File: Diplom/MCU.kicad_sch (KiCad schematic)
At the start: 50 parts, among them IC1 E22-900T22D, J2 Conn_01x04_Pin, SW1 SW_Push, SW2 SW_Push, U2 BME280, U3 W25Q32JVSS, U6 STM32F411CEUx, Y3 ABM3-25.000MHz-D2Y-T, Y4 KX-327NHT, Y5 Crystal

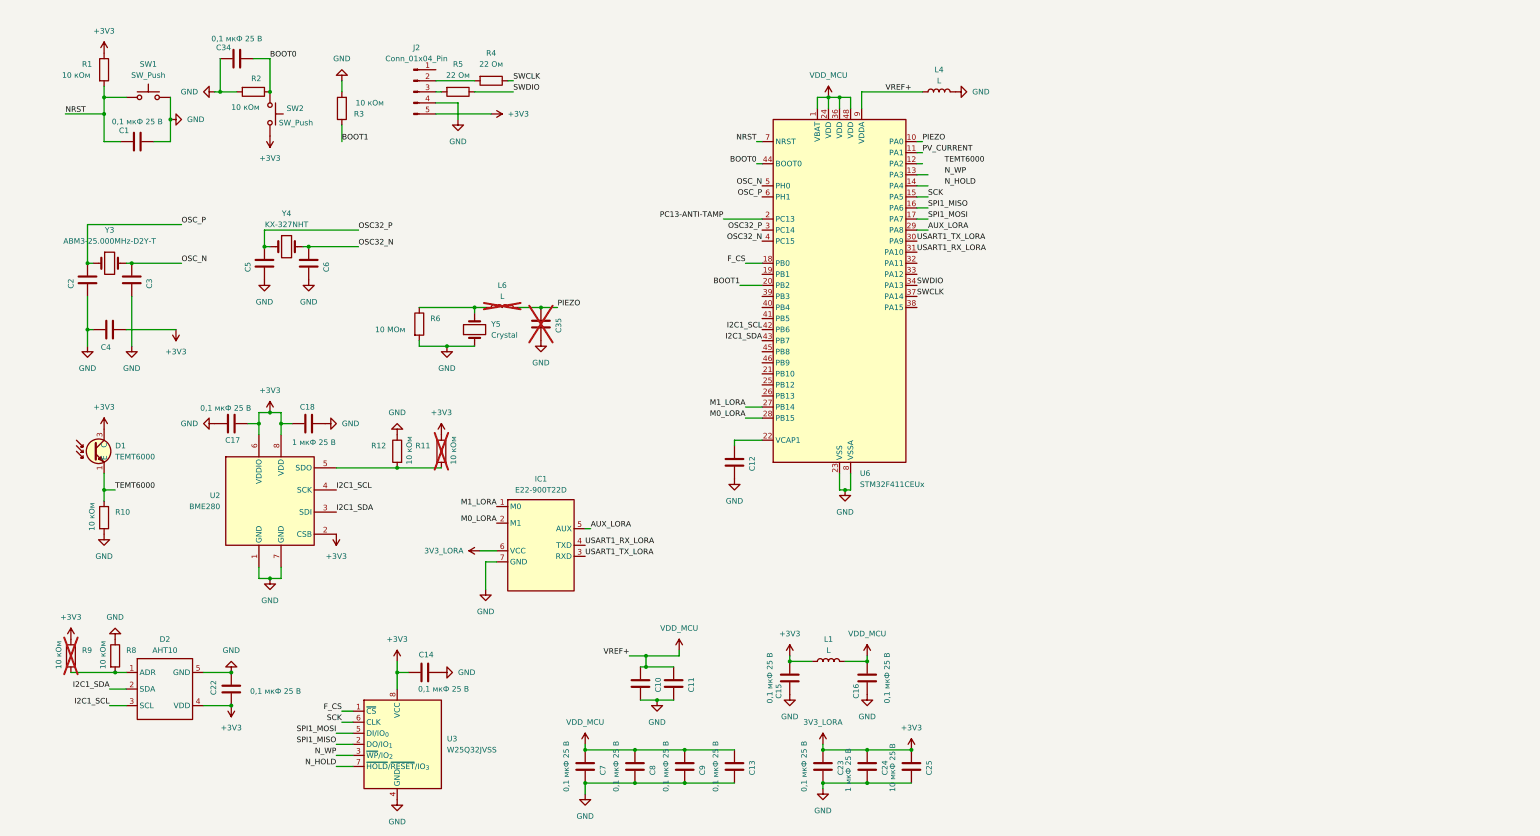
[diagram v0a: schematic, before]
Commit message: version 2.0 fix buttons, roots, tighten dimension
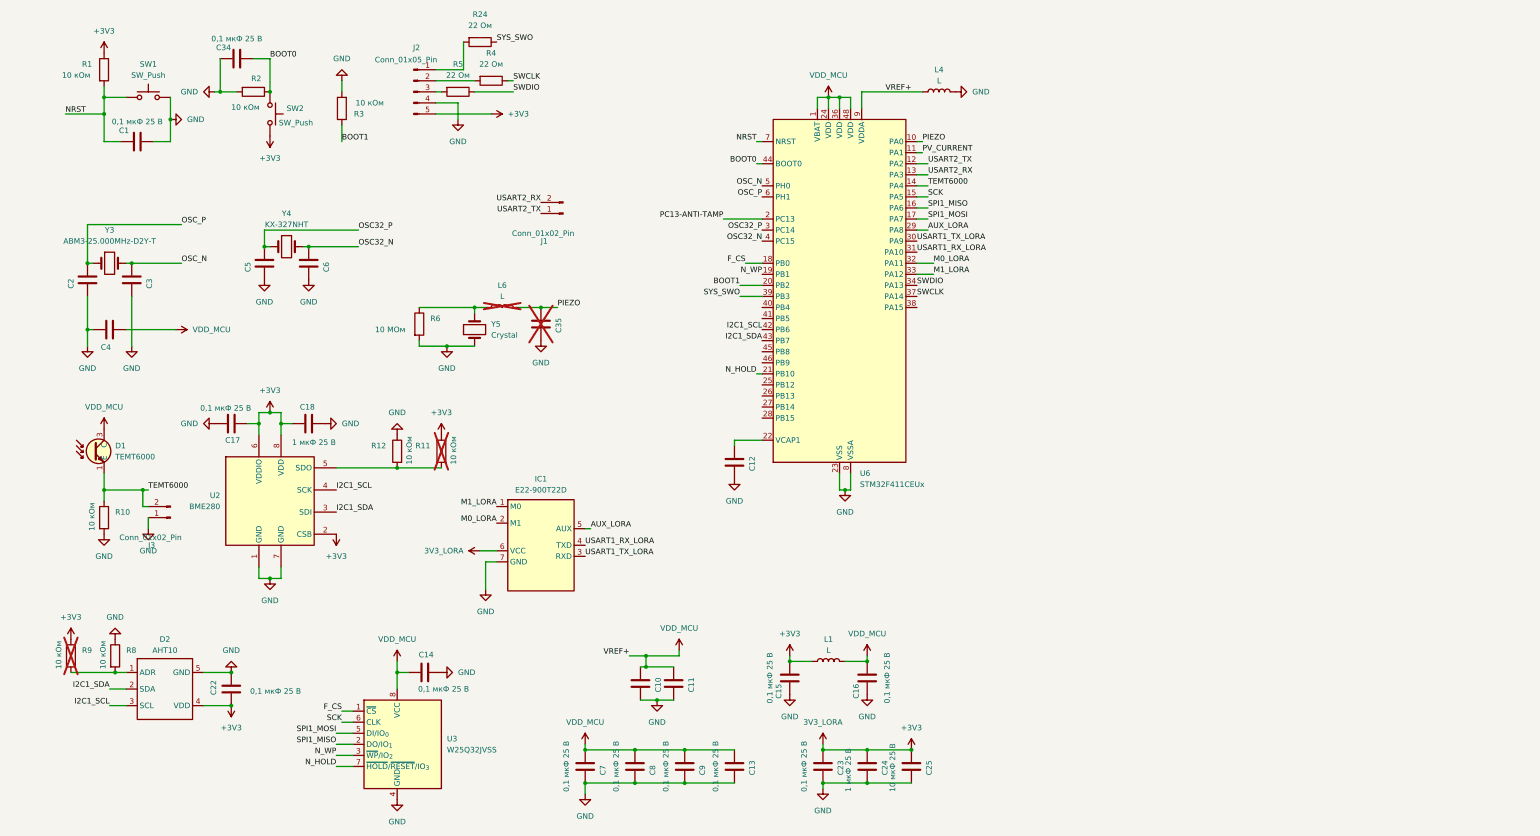
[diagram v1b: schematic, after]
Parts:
- added J1, J3: Conn_01x02_Pin, Connector_PinHeader_2.54mm:PinHeader_1x02_P2.54mm_Vertical, symbol Connector:Conn_01x02_Pin
- added R24: 22 Ом, Resistor_SMD:R_0603_1608Metric_Pad0.98x0.95mm_HandSolder, symbol Device:R
- J2: value Conn_01x04_Pin -> Conn_01x05_Pin; footprint Connector_PinHeader_2.54mm:PinHeader_1x04_P2.54mm_Vertical -> Connector_PinHeader_2.54mm:PinHeader_1x05_P2.54mm_Vertical
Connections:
- net +3V3: no longer C14.1, C4.1, D1.3 (C), U3.8 (VCC)
- net GND: now also J3.1 (Pin_1)
- net M0_LORA: now also U6.32 (PA11); no longer U6.28 (PB15)
- net M1_LORA: now also U6.33 (PA12); no longer U6.27 (PB14)
- net N_HOLD: now also U6.21 (PB10)
- net N_WP: now also U6.19 (PB1)
- net TEMT6000: now also U6.14 (PA4), J3.2 (Pin_2)
- net VDD_MCU: now also C14.1, C4.1, D1.3 (C), U3.8 (VCC)
- net USART2_TX: now reaches U6.12 (PA2)
- net USART2_TX: now also J1.1 (Pin_1)
- net USART2_RX: now reaches U6.13 (PA3)
- net USART2_RX: now also J1.2 (Pin_2)
- net SYS_SWO: now reaches U6.39 (PB3)
- net SYS_SWO: now also R24.1
- net at J2.1 (Pin_1): now also R24.2

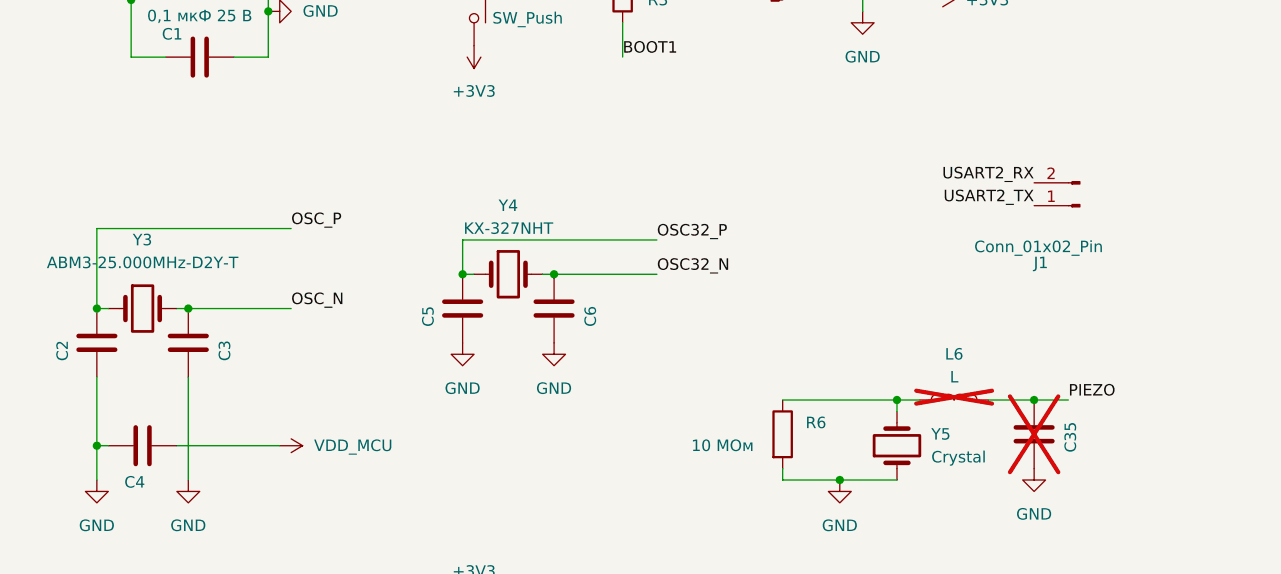
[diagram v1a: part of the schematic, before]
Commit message: Add gitmodule, corrections
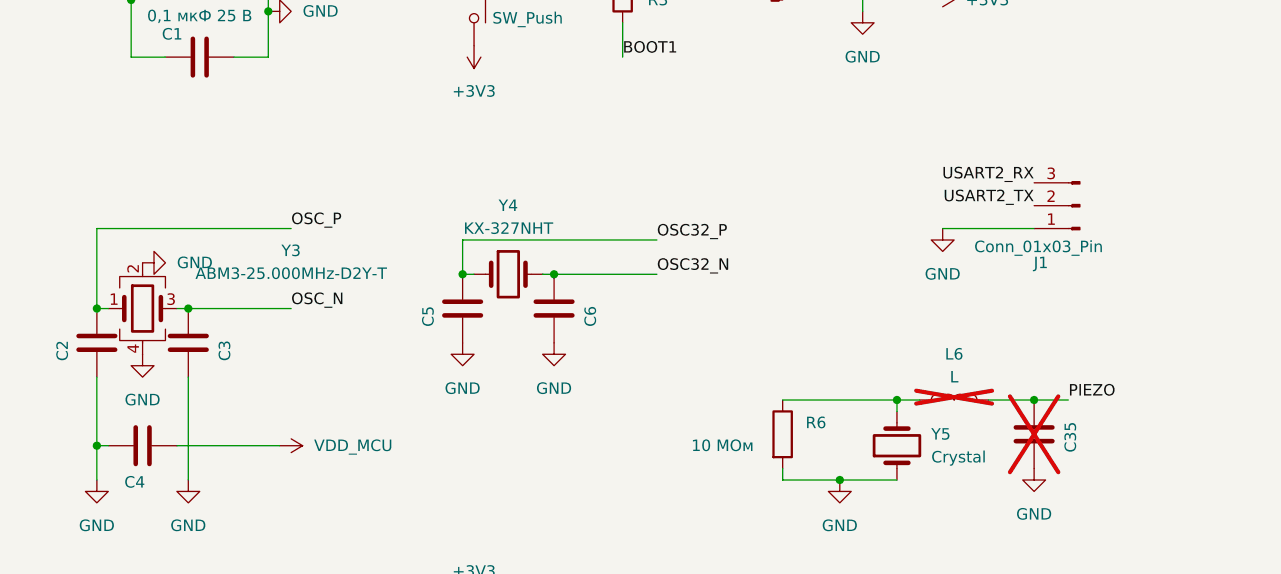
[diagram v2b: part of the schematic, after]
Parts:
- J1: value Conn_01x02_Pin -> Conn_01x03_Pin; footprint Connector_PinHeader_2.54mm:PinHeader_1x02_P2.54mm_Vertical -> Connector_PinHeader_2.54mm:PinHeader_1x03_P2.54mm_Vertical; symbol Connector:Conn_01x02_Pin -> Connector:Conn_01x03_Pin
- SW1, SW2: footprint Button_Switch_THT:SW_PUSH_6mm_H7.3mm -> Diplom:FSM8JSMATR
- Y3: footprint Crystal:Crystal_SMD_3225-4Pin_3.2x2.5mm_HandSoldering -> Crystal:Crystal_SMD_3225-4Pin_3.2x2.5mm; symbol Device:Crystal -> Device:Crystal_GND24
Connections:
- net GND: now also J1.1 (Pin_1), Y3.2, Y3.4
- net OSC_N: now also Y3.3; no longer Y3.2
- net USART2_RX: now also J1.3 (Pin_3); no longer J1.2 (Pin_2)
- net USART2_TX: now also J1.2 (Pin_2); no longer J1.1 (Pin_1)
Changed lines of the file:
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@@
 	(wire
 		(pts
+			(xy 121.92 67.31) (xy 132.08 67.31)
+		)
+		(stroke
+			(width 0)
+			(type default)
+		)
+	)
+	(wire
+		(pts
 			(xy 158.75 176.53) (xy 162.56 176.53)
 		)
@@
 			)
 		)
-		(property "Footprint" "Button_Switch_THT:SW_PUSH_6mm_H7.3mm"
+		(property "Footprint" "Diplom:FSM8JSMATR"
 			(at 74.93 41.91 0)
 			(effects
@@
 			)
 		)
-		(property "Footprint" "Button_Switch_THT:SW_PUSH_6mm_H7.3mm"
+		(property "Footprint" "Diplom:FSM8JSMATR"
 			(at 41.91 33.02 0)
 			(effects
@@
 	)
 	(symbol
+		(lib_id "power:GND")
+		(at 33.02 81.28 0)
+		(unit 1)
+		(exclude_from_sim no)
+		(in_bom yes)
+		(on_board yes)
+		(dnp no)
+		(fields_autoplaced yes)
+		(property "Reference" "#PWR061"
+			(at 33.02 87.63 0)
+			(effects
+				(font
+					(size 1.27 1.27)
+				)
+				(hide yes)
+			)
+		)
+		(property "Value" "GND"
+			(at 33.02 86.36 0)
+			(effects
+				(font
+					(size 1.27 1.27)
+				)
+			)
+		)
+		(property "Footprint" ""
+			(at 33.02 81.28 0)
+			(effects
+				(font
+					(size 1.27 1.27)
+				)
+				(hide yes)
+			)
+		)
+		(property "Datasheet" ""
+			(at 33.02 81.28 0)
+			(effects
+				(font
+					(size 1.27 1.27)
+				)
+				(hide yes)
+			)
+		)
+		(property "Description" "Power symbol creates a global label with name \"GND\" , ground"
+			(at 33.02 81.28 0)
+			(effects
+				(font
+					(size 1.27 1.27)
+				)
+				(hide yes)
+			)
+		)
+		(pin "1"
+		)
+		(instances
+			(project "Diplom"
+				(path "/c3b9ff52-a8d6-450c-a11b-f6a6738b7917/f19e7439-0709-4f6f-9ba2-8e4e7d5c3f4b"
+					(reference "#PWR061")
+					(unit 1)
+				)
+			)
+		)
+	)
+	(symbol
 		(lib_id "Device:R")
 		(at 109.22 119.38 0)
@@
 	)
 	(symbol
-		(lib_id "Device:Crystal")
+		(lib_id "Device:Crystal_GND24")
 		(at 33.02 76.2 0)
 		(unit 1)
@@
 		(fields_autoplaced yes)
 		(property "Reference" "Y3"
-			(at 33.02 68.58 0)
+			(at 49.53 69.7798 0)
 			(effects
 				(font
@@
 		)
 		(property "Value" "ABM3-25.000MHz-D2Y-T"
-			(at 33.02 71.12 0)
+			(at 49.53 72.3198 0)
 			(effects
 				(font
@@
 			)
 		)
-		(property "Footprint" "Crystal:Crystal_SMD_3225-4Pin_3.2x2.5mm_HandSoldering"
+		(property "Footprint" "Crystal:Crystal_SMD_3225-4Pin_3.2x2.5mm"
 			(at 33.02 76.2 0)
 			(effects
@@
 			)
 		)
-		(property "Description" "Two pin crystal 8 MHz"
+		(property "Description" "Four pin crystal, GND on pins 2 and 4"
 			(at 33.02 76.2 0)
 			(effects
@@
 		(pin "1"
 		)
+		(pin "4"
+		)
+		(pin "3"
+		)
 		(instances
 			(project "Diplom"
@@
 	(symbol
 		(lib_id "power:GND")
+		(at 33.02 71.12 90)
+		(unit 1)
+		(exclude_from_sim no)
+		(in_bom yes)
+		(on_board yes)
+		(dnp no)
+		(fields_autoplaced yes)
+		(property "Reference" "#PWR062"
+			(at 39.37 71.12 0)
+			(effects
+				(font
+					(size 1.27 1.27)
+				)
+				(hide yes)
+			)
+		)
+		(property "Value" "GND"
+			(at 36.83 71.1199 90)
+			(effects
+				(font
+					(size 1.27 1.27)
+				)
+				(justify right)
+			)
+		)
+		(property "Footprint" ""
+			(at 33.02 71.12 0)
+			(effects
+				(font
+					(size 1.27 1.27)
+				)
+				(hide yes)
+			)
+		)
+		(property "Datasheet" ""
+			(at 33.02 71.12 0)
+			(effects
+				(font
+					(size 1.27 1.27)
+				)
+				(hide yes)
+			)
+		)
+		(property "Description" "Power symbol creates a global label with name \"GND\" , ground"
+			(at 33.02 71.12 0)
+			(effects
+				(font
+					(size 1.27 1.27)
+				)
+				(hide yes)
+			)
+		)
+		(pin "1"
+		)
+		(instances
+			(project "Diplom"
+				(path "/c3b9ff52-a8d6-450c-a11b-f6a6738b7917/f19e7439-0709-4f6f-9ba2-8e4e7d5c3f4b"
+					(reference "#PWR062")
+					(unit 1)
+				)
+			)
+		)
+	)
+	(symbol
+		(lib_id "power:GND")
 		(at 69.85 148.59 0)
 		(unit 1)
@@
 	)
 	(symbol
+		(lib_id "power:GND")
+		(at 121.92 67.31 0)
+		(unit 1)
+		(exclude_from_sim no)
+		(in_bom yes)
+		(on_board yes)
+		(dnp no)
+		(fields_autoplaced yes)
+		(property "Reference" "#PWR063"
+			(at 121.92 73.66 0)
+			(effects
+				(font
+					(size 1.27 1.27)
+				)
+				(hide yes)
+			)
+		)
+		(property "Value" "GND"
+			(at 121.92 72.39 0)
+			(effects
+				(font
+					(size 1.27 1.27)
+				)
+			)
+		)
+		(property "Footprint" ""
+			(at 121.92 67.31 0)
+			(effects
+				(font
+					(size 1.27 1.27)
+				)
+				(hide yes)
+			)
+		)
+		(property "Datasheet" ""
+			(at 121.92 67.31 0)
+			(effects
+				(font
+					(size 1.27 1.27)
+				)
+				(hide yes)
+			)
+		)
+		(property "Description" "Power symbol creates a global label with name \"GND\" , ground"
+			(at 121.92 67.31 0)
+			(effects
+				(font
+					(size 1.27 1.27)
+				)
+				(hide yes)
+			)
+		)
+		(pin "1"
+		)
+		(instances
+			(project "Diplom"
+				(path "/c3b9ff52-a8d6-450c-a11b-f6a6738b7917/f19e7439-0709-4f6f-9ba2-8e4e7d5c3f4b"
+					(reference "#PWR063")
+					(unit 1)
+				)
+			)
+		)
+	)
+	(symbol
 		(lib_id "Device:L")
 		(at 223.52 36.83 90)
@@
 	)
 	(symbol
-		(lib_id "Connector:Conn_01x02_Pin")
+		(lib_id "Connector:Conn_01x03_Pin")
 		(at 137.16 64.77 180)
 		(unit 1)
@@
 			)
 		)
-		(property "Value" "Conn_01x02_Pin"
+		(property "Value" "Conn_01x03_Pin"
 			(at 132.588 69.342 0)
 			(effects
@@
 			)
 		)
-		(property "Footprint" "Connector_PinHeader_2.54mm:PinHeader_1x02_P2.54mm_Vertical"
+		(property "Footprint" "Connector_PinHeader_2.54mm:PinHeader_1x03_P2.54mm_Vertical"
 			(at 137.16 64.77 0)
 			(effects
@@
 			)
 		)
-		(property "Description" "Generic connector, single row, 01x02, script generated"
+		(property "Description" "Generic connector, single row, 01x03, script generated"
 			(at 137.16 64.77 0)
 			(effects
@@
 		(pin "2"
 		)
+		(pin "3"
+		)
 		(instances

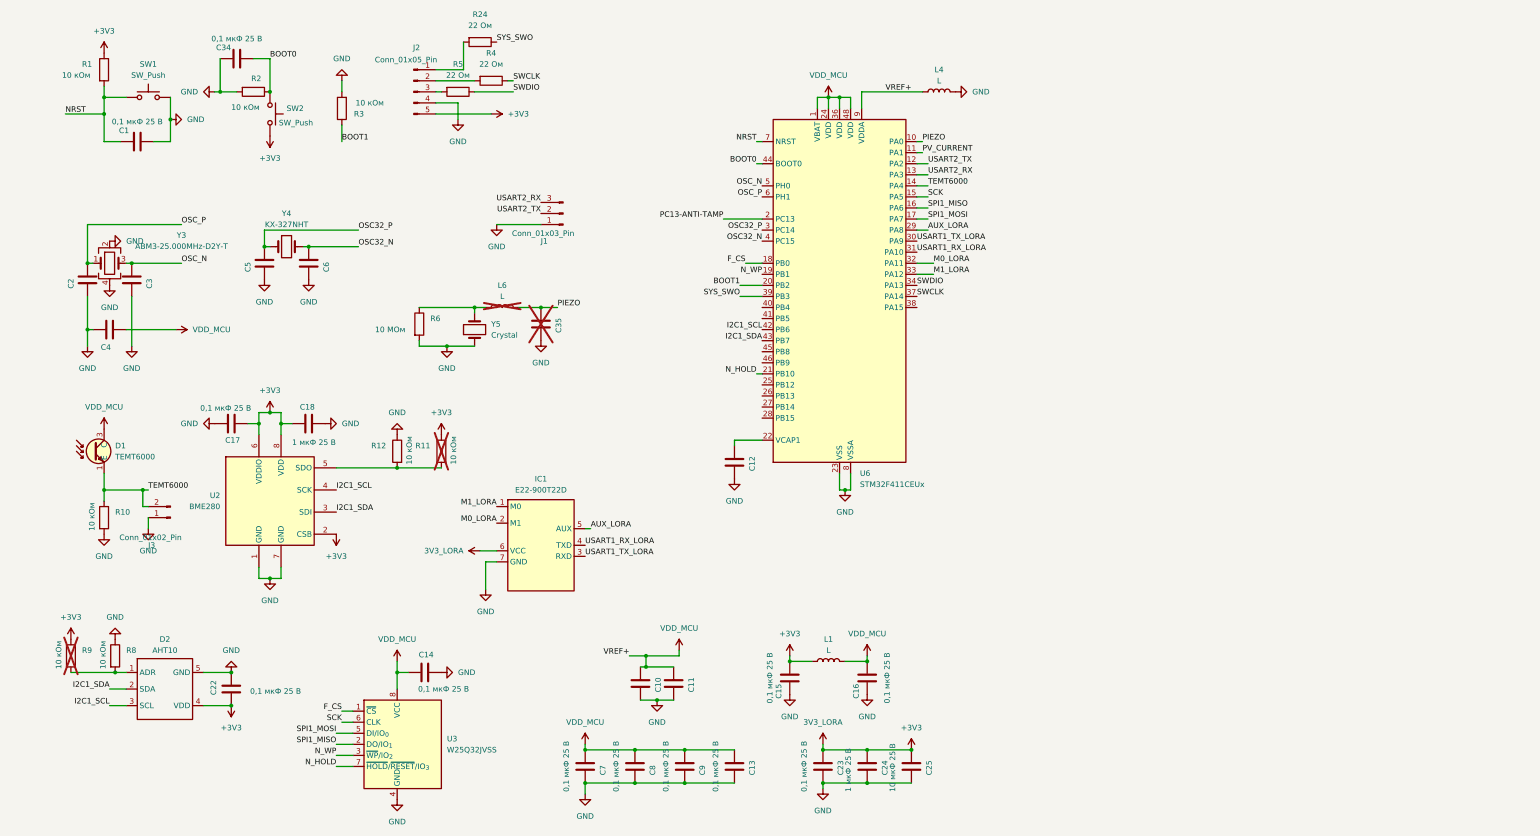
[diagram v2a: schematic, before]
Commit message: LSM6 added, fixes
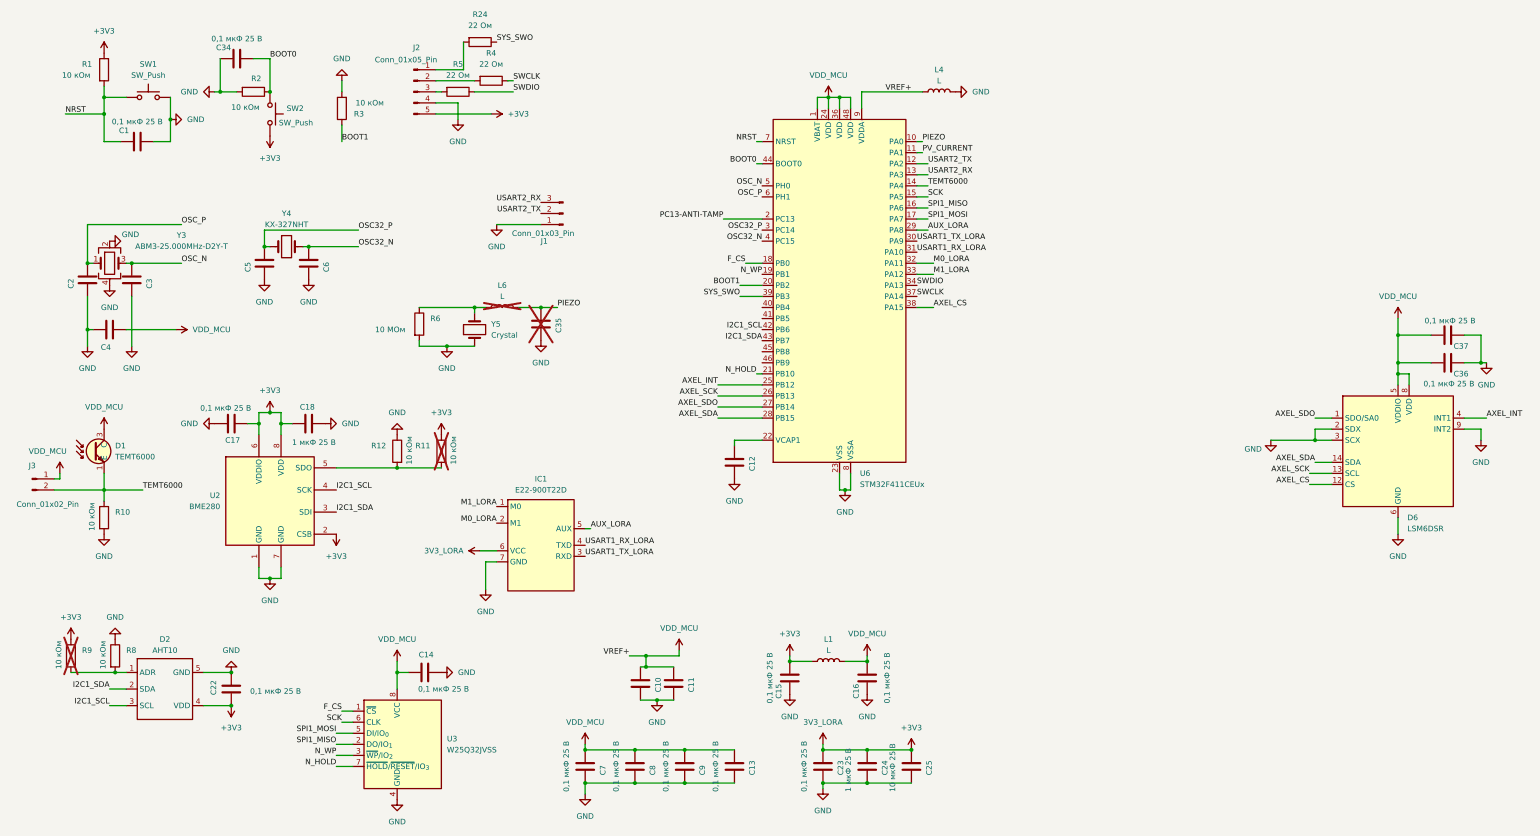
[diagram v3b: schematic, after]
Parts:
- added C36, C37: 0,1 мкФ 25 В, Capacitor_SMD:C_0603_1608Metric_Pad1.08x0.95mm_HandSolder, symbol Device:C
- added D6: LSM6DSR, Package_LGA:LGA-14_3x2.5mm_P0.5mm_LayoutBorder3x4y, symbol Diplom:LSM6DSR
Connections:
- net GND: now also C36.1, C37.1, D6.2 (SDX), D6.3 (SCX), D6.6 (GND), D6.7 (GND), D6.9 (INT2); no longer J3.1 (Pin_1)
- net VDD_MCU: now also J3.1 (Pin_1), C36.2, C37.2, D6.5 (VDDIO), D6.8 (VDD)
- net AXEL_INT: now reaches U6.25 (PB12)
- net AXEL_INT: now also D6.4 (INT1)
- net AXEL_SCK: now reaches U6.26 (PB13)
- net AXEL_SCK: now also D6.13 (SCL)
- net AXEL_SDO: now reaches U6.27 (PB14)
- net AXEL_SDO: now also D6.1 (SDO/SA0)
- net AXEL_SDA: now reaches U6.28 (PB15)
- net AXEL_SDA: now also D6.14 (SDA)
- net AXEL_CS: now reaches U6.38 (PA15)
- net AXEL_CS: now also D6.12 (CS)
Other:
- moved on the sheet: J3
